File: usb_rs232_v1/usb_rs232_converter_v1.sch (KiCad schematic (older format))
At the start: 5 parts, among them CON1 USB-MINI-B, CON2 USB-MICRO-B, J1 DB9, J2 DB9

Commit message: Dodane biblioteki z sieci
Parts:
- removed I1: FT232BM, symbol FT232BM
- added I1: FT232BL, ~, symbol FT232BL
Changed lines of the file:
@@
 LIBS:valves
 LIBS:m_edit
+LIBS:usb_rs232_converter_v1-cache
 EELAYER 27 0
 EELAYER END
@@
 Comment4 ""
 $EndDescr
-$Comp
-L FT232BM I1
-U 1 1 556E290F
-P 3650 2700
-F 0 "I1" H 4150 4100 60  0000 C CNN
-F 1 "FT232BM" H 4250 1300 60  0000 C CNN
-F 2 "" H 3650 2700 60  0000 C CNN
-F 3 "" H 3650 2700 60  0000 C CNN
-	1    3650 2700
-	1    0    0    -1
-$EndComp
 $Comp
 L DB9 J1
@@
 	1    0    0    -1
 $EndComp
+$Comp
+L FT232BL I1
+U 1 1 556F35D9
+P 3300 3100
+F 0 "I1" H 3750 4550 60  0000 C CNN
+F 1 "FT232BL" H 3850 1750 60  0000 C CNN
+F 2 "~" H 3250 3150 60  0000 C CNN
+F 3 "~" H 3250 3150 60  0000 C CNN
+	1    3300 3100
+	1    0    0    -1
+$EndComp

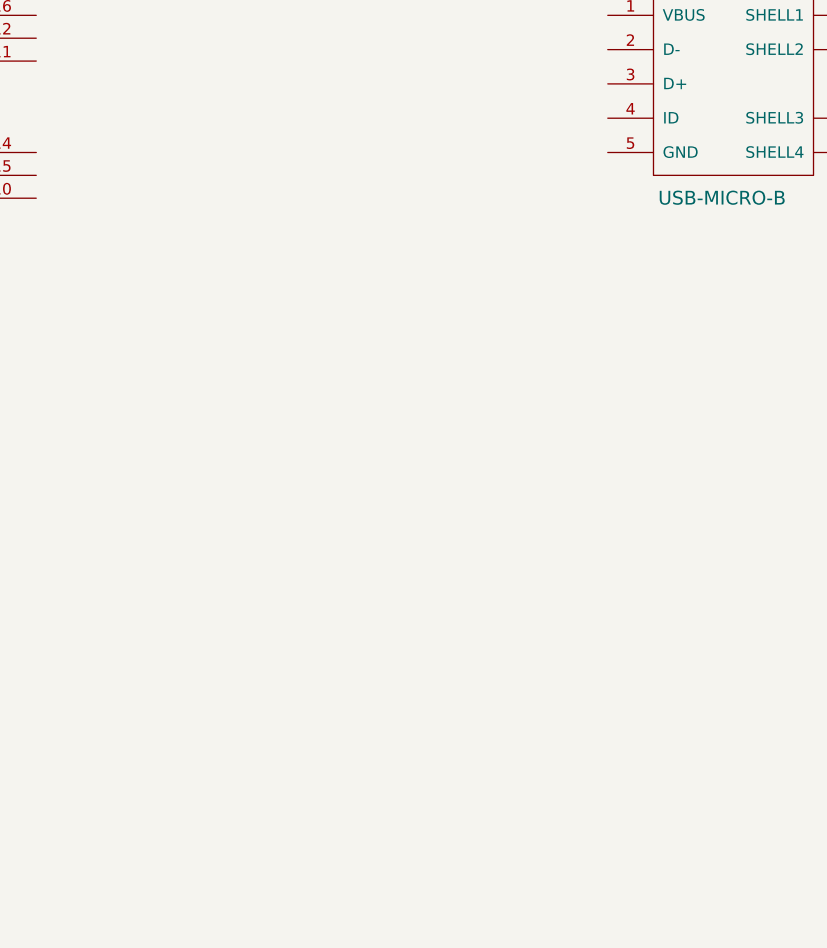
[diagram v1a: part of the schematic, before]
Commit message: Sprawdzone footprinty
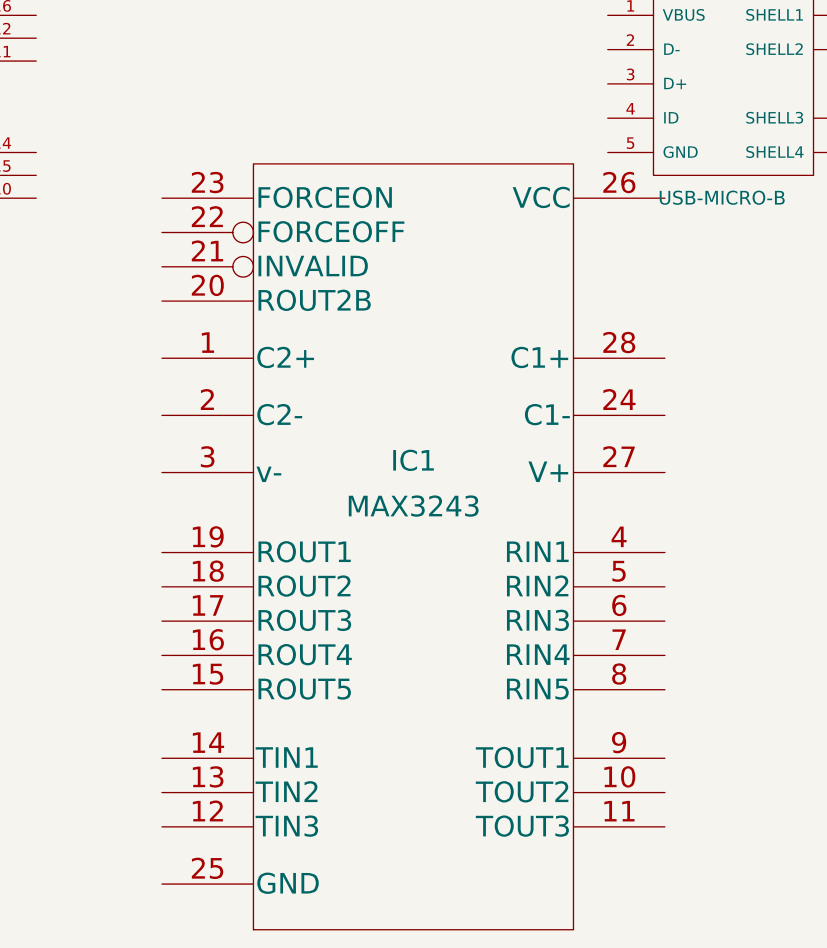
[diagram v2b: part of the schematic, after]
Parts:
- added IC1: MAX3243, symbol MAX3243
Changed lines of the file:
@@
+	1    0    0    -1
+$EndComp
+$Comp
+L MAX3243 IC1
+U 1 1 556F7406
+P 6000 5600
+F 0 "IC1" H 6000 6050 90  0000 C CNN
+F 1 "MAX3243" H 6000 5850 90  0000 C CNN
+F 2 "" H 6000 5600 60  0000 C CNN
+F 3 "" H 6000 5600 60  0000 C CNN
+	1    6000 5600
 	1    0    0    -1
 $EndComp

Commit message: Schemat v1
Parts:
- removed IC1: MAX3243, symbol MAX3243
- added C? (x4): C, ~, symbol C
- added C? (x4): 100n, ~, symbol C
- added C?: 33n, ~, symbol C
- added C?: 10n, ~, symbol C
- added C? (x2): 10u, ~, symbol CP1
- added COM (x4), RS232: HDR-1X8-SIP-100, con-hdrs40-SIP-100-8V, symbol HDR-1X8-SIP-100
- added D? (x3): GREEN, ~, symbol LED
- added D? (x3): RED, ~, symbol LED
- added D? (x12): YELLOW, ~, symbol LED
- added F? (x2): 500mA, ~, symbol FUSE
- added IC?: MAX3243, ~, symbol MAX3243
- added L?: INDUCTOR_SMALL, ~, symbol INDUCTOR_SMALL
- added R? (x2): 27R, ~, symbol R
- added R?: 1k5, ~, symbol R
- added R? (x17): 470R, ~, symbol R
- added R? (x2): R, ~, symbol R
- added UART: HDR-1X4-SIP-100, con-hdrs40-SIP-100-4V, symbol HDR-1X4-SIP-100
- J1: value DB9 -> COM LEFT
- J2: value DB9 -> COM RIGHT
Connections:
- net at J1.1: now also COM.7, D?.2 (K)
- net at J1.2: now also COM.2, D?.2 (K)
- net at J1.3: now also COM.1, D?.2 (K)
- net at J1.4: now also COM.5, D?.2 (K)
- net GND: now reaches J1.5
- net GND: now also I1.14 (PWRCTL), I1.17 (GND), I1.29 (AGND), I1.9 (GND), J2.5, C?.1, C?.1, C?.1, C?.2, C?.2, C?.2, C?.2, C?.2, C?.2, F?.1, IC?.25 (GND), R?.2, R?.2, R?.2, R?.2, R?.2, R?.2, R?.2, R?.2, R?.2, R?.2, R?.2, R?.2, R?.2, R?.2, R?.2, R?.2, UART.4
- net at J1.6 (P6): now also COM.6, D?.2 (K)
- net at J1.7 (P7): now also COM.3, D?.2 (K)
- net at J1.8 (P8): now also COM.4, D?.2 (K)
- net at J1.9 (P9): now also COM.8, D?.2 (K)
- net R7: now reaches J2.1
- net R7: now also COM.7, COM.7, COM.7, D?.2 (K)
- net R2: now reaches J2.2
- net R2: now also COM.2, COM.2, COM.2, D?.2 (K)
- net R1: now reaches J2.3
- net R1: now also COM.1, COM.1, COM.1, D?.2 (K)
- net R5: now reaches J2.4
- net R5: now also COM.5, COM.5, COM.5, D?.2 (K)
- net R6: now reaches J2.6 (P6)
- net R6: now also COM.6, COM.6, COM.6, D?.2 (K)
- net R3: now reaches J2.7 (P7)
- net R3: now also COM.3, COM.3, COM.3, D?.2 (K)
- net R4: now reaches J2.8 (P8)
- net R4: now also COM.4, COM.4, COM.4, D?.2 (K)
- net R8: now reaches J2.9 (P9)
- net R8: now also COM.8, COM.8, COM.8, D?.2 (K)
- net at CON1.1 (VBUS): now also CON2.1 (VBUS), F?.1
- net at CON1.2 (D-): now also CON2.2 (D-), R?.1
- net at CON1.3 (D+): now also CON2.3 (D+), R?.1
- net at CON1.5 (GND): now also CON2.5 (GND), F?.2
- net at I1.11 (~RXLED): now also R?.2
- net at I1.12 (~TXLED): now also R?.2
- net at I1.13 (VCCIO): now also I1.26 (VCC), I1.3 (VCC), L?.2, R?.1
- net at I1.18 (D7/~RI): now also IC?.15 (ROUT5)
- net at I1.19 (D6/~DCD): now also IC?.16 (ROUT4)
- net at I1.20 (D5/~DSR): now also IC?.17 (ROUT3)
- net at I1.21 (D4/~DTR): now also IC?.12 (TIN3)
- net at I1.22 (D3/~CTS): now also IC?.18 (ROUT2)
- net at I1.23 (D2/~RST): now also IC?.13 (TIN2)
- net at I1.24 (D1/RXD): now also IC?.19 (ROUT1), UART.3
- net at I1.25 (D0/TXD): now also IC?.14 (TIN1), UART.2
- net at I1.30 (AVCC): now also C?.2, R?.2
- net VCC: now reaches I1.4 (~RESET)
- net VCC: now also C?.1, C?.1, C?.1, C?.1, C?.1, C?.1, C?.2, D?.1 (A), D?.1 (A), F?.2, IC?.22 (FORCEOFF), IC?.23 (FORCEON), IC?.26 (VCC), L?.1, UART.1
- net at I1.5 (~RSTOUT): now also R?.1
- net at I1.6 (3V3OUT): now also C?.2
- net at I1.7 (USBDP): now also R?.2, R?.2
- net at I1.8 (USBDM): now also R?.2
- new net: D?.2 (K), R?.1 (x2)
- new net: D?.1 (A), R?.1 (x16)
- new net: C?.1, IC?.2 (C2-)
- new net: C?.2, IC?.1 (C2+)
- new net: C?.2, IC?.3 (v-)
- new net: C?.1, IC?.28 (C1+)
- new net: C?.2, IC?.24 (C1-)
- new net: C?.1, IC?.27 (V+)
- new net CTS: IC?.5 (RIN2), RS232.4
- new net DCD: IC?.7 (RIN4), RS232.7
- new net DSR: IC?.6 (RIN3), RS232.6
- new net DTR: IC?.11 (TOUT3), RS232.5
- new net RI: IC?.8 (RIN5), RS232.8
- new net RST: IC?.10 (TOUT2), RS232.3
- new net RxD: IC?.4 (RIN1), RS232.2
- new net TxD: IC?.9 (TOUT1), RS232.1
- no-connect marks 0 -> 21
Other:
- moved on the sheet: CON1, CON2, I1, J1, J2

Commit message: Pcb v0.1
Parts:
- removed D?: RED, ~, symbol LED
- removed D?: GREEN, ~, symbol LED
- removed D? (x6): YELLOW, ~, symbol LED
- removed R? (x8): 470R, ~, symbol R
- added J5: UART OSC, con-hdrs40-SIP-100-2V, symbol HDR-1X2-SIP-100
- COM1: renamed from COM; value HDR-1X8-SIP-100 -> COM LEFT COM
- COM2: renamed from COM; value HDR-1X8-SIP-100 -> COM RIGHT COM
- COM3: renamed from COM; value HDR-1X8-SIP-100 -> COM RIGHT FTDI
- COM4: renamed from COM; value HDR-1X8-SIP-100 -> COM RIGHT OSC
- J3: renamed from RS232; value HDR-1X8-SIP-100 -> FTDI
- J4: renamed from UART; value HDR-1X4-SIP-100 -> UART
- gave numbers to parts that had none: 40
- renumbered I1 to IC2
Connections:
- wire segments 215 -> 201
- no-connect marks 21 -> 22
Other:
- moved on the sheet: C1, C2, C3, C6

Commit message: Pcb v0.2
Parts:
- removed C1: 100n, ~, symbol C
- removed C6: 10n, ~, symbol C
- removed COM4: COM RIGHT OSC, con-hdrs40-SIP-100-8V, symbol HDR-1X8-SIP-100
- removed CON2: USB-MICRO-B, symbol USB-MINI-B
- removed F1, F2: 500mA, ~, symbol FUSE
- removed J5: UART OSC, con-hdrs40-SIP-100-2V, symbol HDR-1X2-SIP-100
- added R7: 0R, ~, symbol R
- CON1: value USB-MINI-B -> USB-micro-B
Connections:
- net labels added: CTS COM, CTS COM LEFT, D+, D++, D-, D--, DCD COM, DCD COM LEFT, DSR COM, DSR COM LEFT, DTR COM, DTR COM LEFT, RI COM, RI COM LEFT, RST COM, RST COM LEFT, RX LED, Rin: CTS, Rin: DCD, Rin: DSR, Rin: RI, Rin: RxD, Rout: CTS, Rout: DCD, Rout: DSR, Rout: RI, Rout: RxD, RxD COM, RxD COM LEFT, TX LED, Tin: DTR, Tin: RST, Tin: RST2, Tin: TxD, Tout: DTR, Tout: RST, Tout: TxD, TxD COM, TxD COM LEFT, USB Vcc
- net labels removed: CTS, DCD, DSR, DTR, R1, R2, R3, R4, R5, R6, R7, R8, RI, RST, RxD, TxD
- wire segments 201 -> 173
- no-connect marks 22 -> 17
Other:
- moved on the sheet: C10, C11, C2, C3, C4, C5, C7, C8, COM1, COM2, COM3, D1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

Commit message: PCB v1.0 BIG
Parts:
- added CON2: USB-mini-B, symbol USB-MINI-B
- added F1: FUSE, ~, symbol FUSE
- added R10, R11, R8, R9: 0R, ~, symbol R
- renumbered COM3 to J4, J4 to J5, COM1 to J6, COM2 to J7
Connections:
- net D+: now also CON2.3 (D+)
- net D-: now also CON1.2 (D-), CON2.2 (D-); no longer CON1.4 (ID)
- net DCD COM: now also J4.2, J7.2; no longer J4.7, J7.7
- net DCD COM LEFT: now also J6.2; no longer J6.7
- net DSR COM: now also J4.3, J7.3; no longer J4.6, J7.6
- net DSR COM LEFT: now also J6.3; no longer J6.6
- net DTR COM: now also J4.7, J7.7; no longer J4.5, J7.5
- net DTR COM LEFT: now also J6.7; no longer J6.5
- net GND: now also R10.1, R9.1; no longer CON1.1 (VBUS)
- net RI COM: now also J4.1, J7.1; no longer J4.8, J7.8
- net RI COM LEFT: now also J6.1; no longer J6.8
- net RST COM: now also J4.8, J7.8; no longer J4.3, J7.3
- net RST COM LEFT: now also J6.8; no longer J6.3
- net Rin: DCD: now also J3.2; no longer J3.7
- net Rin: DSR: now also J3.3; no longer J3.6
- net Rin: RI: now also J3.1; no longer J3.8
- net Rin: RxD: now also J3.5; no longer J3.2
- net Rout: RxD: now also R11.1; no longer J5.3
- net RxD COM: now also J4.5, J7.5; no longer J4.2, J7.2
- net RxD COM LEFT: now also J6.5; no longer J6.2
- net Tout: DTR: now also J3.7; no longer J3.5
- net Tout: RST: now also J3.8; no longer J3.3
- net Tout: TxD: now also J3.6; no longer J3.1
- net TxD COM: now also J4.6, J7.6; no longer J4.1, J7.1
- net TxD COM LEFT: now also J6.6; no longer J6.1
- net VCC: now also C3.1
- net USB Vcc renamed PWR FLAG
- net PWR FLAG: now also CON1.1 (VBUS), CON2.1 (VBUS), CON2.5 (GND), F1.1, F1.2, R10.2, R8.1, R8.2, R9.2; no longer C3.1
- new net: J5.3, R11.2
- no-connect marks 17 -> 22
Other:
- moved on the sheet: C2, C3, C9, J3, J4, L1, R1

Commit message: usb_rs232 pcb_v2.0
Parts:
- removed C5: 10u, ~, symbol CP1
- removed J5: UART, con-hdrs40-SIP-100-4V, symbol HDR-1X4-SIP-100
- removed R10, R11, R7, R8, R9: 0R, ~, symbol R
- added C1, C3: 27p, ~, symbol C
- added C13, C14, C16, C7: 100n, ~, symbol C
- added C15: 4n7, ~, symbol C
- added F2: 500mA, ~, symbol FUSE
- added J4: UART, con-hdrs40-SIP-100-5V, symbol HDR-1X5-SIP-100
- added VR1: MC78L33, TO-92, symbol MC78L05AACP
- added X1: QUARTZCMS4_M, ~, symbol QUARTZCMS4_M
- C11: renamed from C8; value C -> 100n
- C12: renamed from C11; value C -> 100n
- C8: renamed from C7; value C -> 100n
- C9: renamed from C10; value C -> 100n
- D10: renamed from D18; value YELLOW -> RI
- D3: renamed from D11; value RED -> TxD
- D4: renamed from D12; value GREEN -> RxD
- D5: renamed from D13; value YELLOW -> RTS
- D6: renamed from D14; value YELLOW -> CTS
- D7: renamed from D15; value YELLOW -> DTR
- D8: renamed from D16; value YELLOW -> DSR
- D9: renamed from D17; value YELLOW -> DCD
- F1: value FUSE -> 500mA
- L1: value INDUCTOR_SMALL -> 15uH
- R10: renamed from R5; value R -> 470R
- R11: renamed from R6; value R -> 470R
- renumbered C4 to C10, C12 to C2, C3 to C4, C9 to C5, C2 to C6, IC2 to IC1, IC1 to IC2, J6 to J2, J7 to J3, J2 to J6, J3 to J7, J4 to J8, R15 to R12, R16 to R13, R17 to R14, R18 to R15, R19 to R16, R20 to R17, R21 to R18, R22 to R19, R2 to R5, R3 to R6, R4 to R7, R1 to R8
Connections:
- net labels added: +3,3V, +5V, AVCC, XTIN, XTOUT
- net labels removed: PWR FLAG, Tin: RST2, USB Vcc, VCC
- wire segments 187 -> 238
- no-connect marks 22 -> 18
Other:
- moved on the sheet: C10, C5, D1, D2, F1, R10, R11, R7

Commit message: usb_rs232: v2.1: poprawiony footprint VR1
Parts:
- removed VR1: MC78L33, TO-92, symbol MC78L05AACP
- added VR1: MC78L33, symbol MC78L33
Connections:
- wire segments 238 -> 203
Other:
- note added: "Można dodać na wyjścia zasilające:\n- diody zenera 3.6, 5.5\n- kondensatorki 100n\n- ewentualnie ferryt"
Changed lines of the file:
@@
 LIBS:ftdichip-2
 LIBS:ftdichip-3
-LIBS:usb_rs232_converter_v1-cache
 EELAYER 27 0
 EELAYER END
@@
 Sheet 1 1
 Title ""
-Date "28 jun 2015"
+Date "7 feb 2016"
 Rev ""
 Comp ""
@@
 $EndComp
 $Comp
-L MC78L05AACP VR1
-U 1 1 558DD6B1
-P 6800 1050
-F 0 "VR1" H 6600 1250 40  0000 C CNN
-F 1 "MC78L33" H 6800 1250 40  0000 L CNN
-F 2 "TO-92" H 6800 1150 30  0000 C CIN
-F 3 "" H 6800 1050 60  0000 C CNN
-	1    6800 1050
-	1    0    0    -1
-$EndComp
-$Comp
 L C C7
 U 1 1 558DD6C3
@@
 Connection ~ 5500 5550
 Wire Wire Line
-	5500 5400 5500 5550
-Wire Wire Line
-	5500 5550 5500 5650
-Wire Wire Line
-	5350 5550 5500 5550
-Wire Wire Line
-	5500 5550 5650 5550
+	5500 5400 5500 5650
+Wire Wire Line
+	5350 5550 5650 5550
 Wire Wire Line
 	5350 5400 5350 5550
@@
 	9750 1900 10050 1900
 Wire Wire Line
-	9750 1800 9750 1900
-Wire Wire Line
-	9750 1900 9750 2050
+	9750 1800 9750 2050
 Wire Wire Line
 	1750 3400 1900 3400
@@
 	5250 1000 5250 1200
 Wire Wire Line
-	5250 1700 5250 1800
-Wire Wire Line
-	5250 1800 5250 2200
-Wire Wire Line
-	4150 2700 4300 2700
-Wire Wire Line
-	4300 2700 4400 2700
+	5250 1700 5250 2200
+Wire Wire Line
+	4150 2700 4400 2700
 Wire Wire Line
 	3650 3150 4400 3150
 Wire Wire Line
-	1750 3100 2300 3100
-Wire Wire Line
-	2300 3100 2800 3100
+	1750 3100 2800 3100
 Wire Wire Line
 	3650 2950 4400 2950
 Wire Wire Line
-	1750 2950 2200 2950
-Wire Wire Line
-	2200 2950 3150 2950
+	1750 2950 3150 2950
 Wire Wire Line
 	7500 9200 7850 9200
@@
 	7500 9300 7500 9500
 Wire Wire Line
-	12000 7300 12000 7550
-Wire Wire Line
-	12000 7550 12000 7800
-Wire Wire Line
-	12000 7800 12000 8050
-Wire Wire Line
-	12000 8050 12000 8350
-Wire Wire Line
-	12000 8350 12000 8650
-Wire Wire Line
-	12000 8650 12000 8950
-Wire Wire Line
-	12000 8950 12000 9250
-Wire Wire Line
-	12000 9250 12000 9550
+	12000 7300 12000 9550
 Wire Wire Line
 	12000 7300 12200 7300
@@
 	6200 9200 6150 9200
 Wire Wire Line
-	1750 4800 1900 4800
-Wire Wire Line
-	1900 3400 1900 3800
-Wire Wire Line
-	1900 3800 1900 4800
-Wire Wire Line
-	1900 4800 1900 5100
-Wire Wire Line
-	1900 5100 1900 5300
+	1900 4800 1750 4800
+Wire Wire Line
+	1900 3400 1900 5300
 Wire Wire Line
 	1750 4350 2200 4350
@@
 Connection ~ 2300 3100
 Wire Wire Line
-	1750 4200 2550 4200
-Wire Wire Line
-	2550 4200 2950 4200
+	1750 4200 2950 4200
 Wire Wire Line
 	4950 2250 4950 2350
@@
 Connection ~ 4500 1000
 Wire Wire Line
-	4200 1000 4500 1000
-Wire Wire Line
-	4500 1000 4950 1000
-Wire Wire Line
-	4950 1000 5250 1000
-Wire Wire Line
-	5250 1000 5550 1000
-Wire Wire Line
-	5550 1000 6050 1000
-Wire Wire Line
-	6050 1000 6300 1000
-Wire Wire Line
-	6300 1000 6400 1000
+	4200 1000 6400 1000
 Wire Wire Line
 	4950 1050 4950 1000
 Connection ~ 4950 1000
 Wire Wire Line
-	2550 2800 2550 4200
-Wire Wire Line
-	2550 4200 2550 4350
+	2550 2800 2550 4350
 Wire Wire Line
 	2950 4200 2950 2400
@@
 	4400 4750 4400 5100
 Wire Wire Line
-	4000 4150 4050 4150
-Wire Wire Line
-	4050 4150 4400 4150
+	4000 4150 4400 4150
 Wire Wire Line
 	4050 4400 4050 4150
@@
 	4400 3950 3300 3950
 Wire Wire Line
-	3300 3950 3300 4150
-Wire Wire Line
-	3300 4150 3300 4350
+	3300 3950 3300 4350
 Wire Wire Line
 	3400 4150 3300 4150
@@
 	8150 4250 8050 4250
 Wire Wire Line
-	8150 3900 8150 4050
-Wire Wire Line
-	8150 4050 8150 4250
+	8150 3900 8150 4250
 Wire Wire Line
 	8050 4050 8150 4050
 Connection ~ 8150 4050
 Wire Wire Line
-	7200 1000 7350 1000
-Wire Wire Line
-	7350 1000 7550 1000
-Wire Wire Line
-	7350 800  7350 1000
-Wire Wire Line
-	7350 1000 7350 1050
+	7200 1000 7550 1000
+Wire Wire Line
+	7350 800  7350 1050
 Wire Wire Line
 	7350 1450 7350 1550
@@
 	6800 1300 6800 1550
 Wire Wire Line
-	5550 800  5550 1000
-Wire Wire Line
-	5550 1000 5550 1800
-Wire Wire Line
-	5550 1800 5550 2200
+	5550 800  5550 2200
 Connection ~ 5550 1000
 Wire Wire Line
@@
 	2550 4750 2550 5100
 Wire Wire Line
-	12950 1650 12950 1900
-Wire Wire Line
-	12950 1900 12950 1950
+	12950 1650 12950 1950
 Connection ~ 12950 1900
 Wire Wire Line
@@
 	550  4200 650  4200
 Wire Wire Line
-	2950 850  2950 1000
-Wire Wire Line
-	2950 1000 2950 1900
+	2950 850  2950 1900
 Wire Wire Line
 	2950 1000 3700 1000
@@
 Connection ~ 550  3800
 Wire Wire Line
-	550  3250 550  3800
-Wire Wire Line
-	550  3800 550  4200
+	550  3250 550  4200
 Wire Wire Line
 	2550 5100 1900 5100
@@
 Wire Wire Line
 	6050 1450 6050 1550
+$Comp
+L MC78L33 VR1
+U 1 1 56B753B5
+P 6800 1050
+F 0 "VR1" H 6600 1250 40  0000 C CNN
+F 1 "MC78L33" H 6800 1250 40  0000 L CNN
+F 2 "" H 7100 700 30  0000 C CIN
+F 3 "" H 6800 1050 60  0000 C CNN
+	1    6800 1050
+	1    0    0    -1
+$EndComp
+Text Notes 7000 2050 0    60   ~ 0
+Można dodać na wyjścia zasilające:\n- diody zenera 3.6, 5.5\n- kondensatorki 100n\n- ewentualnie ferryt
 $EndSCHEMATC
